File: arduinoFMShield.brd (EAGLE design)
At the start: 29.7 x 58.4 mm, 32 parts, among them IC1 ATMEGA168-MU, IC2 FT232RQ, X1 MINI-USB-32005-301, X2 R141426

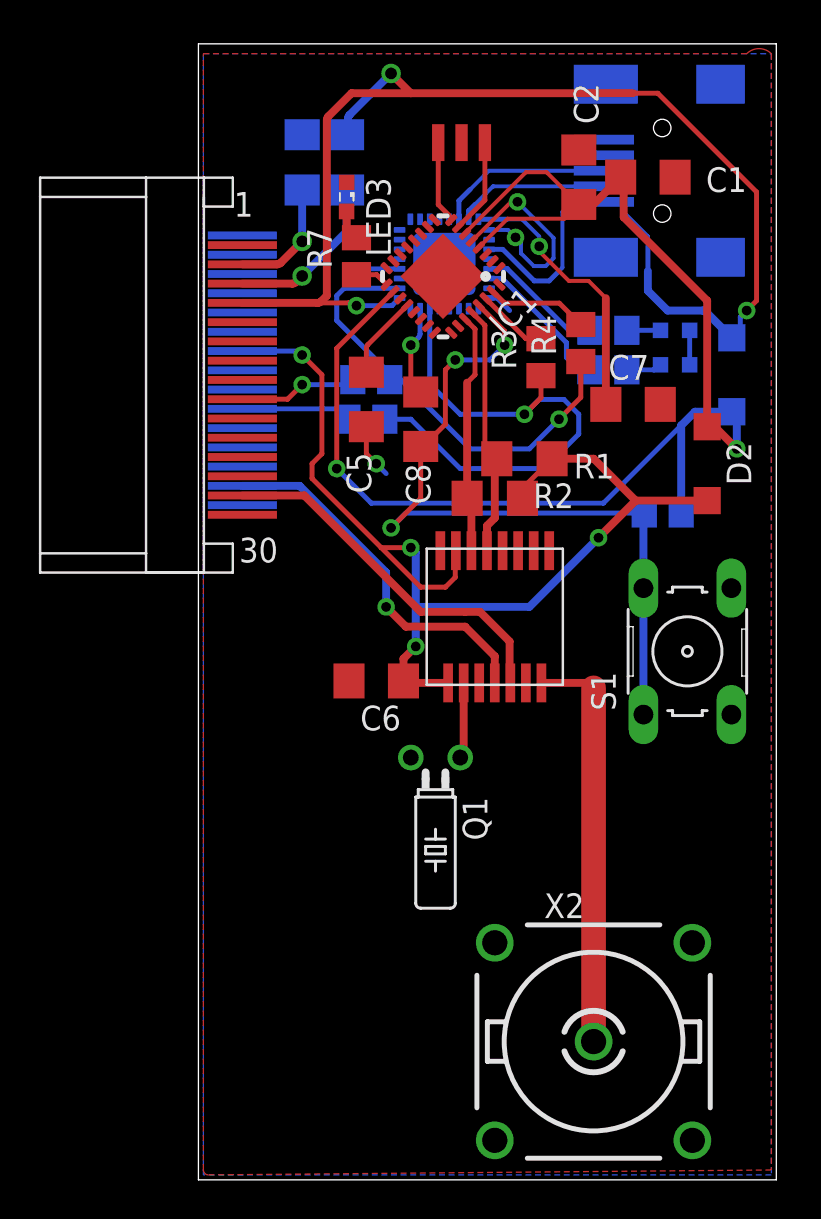
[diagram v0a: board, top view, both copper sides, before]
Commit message: 8/31/2013 Changed FTDI chip and atmega to bigger package for easier soldering. Add murata resonator
Signed-off-by: goose1987 <phamh1987@gmail.com>
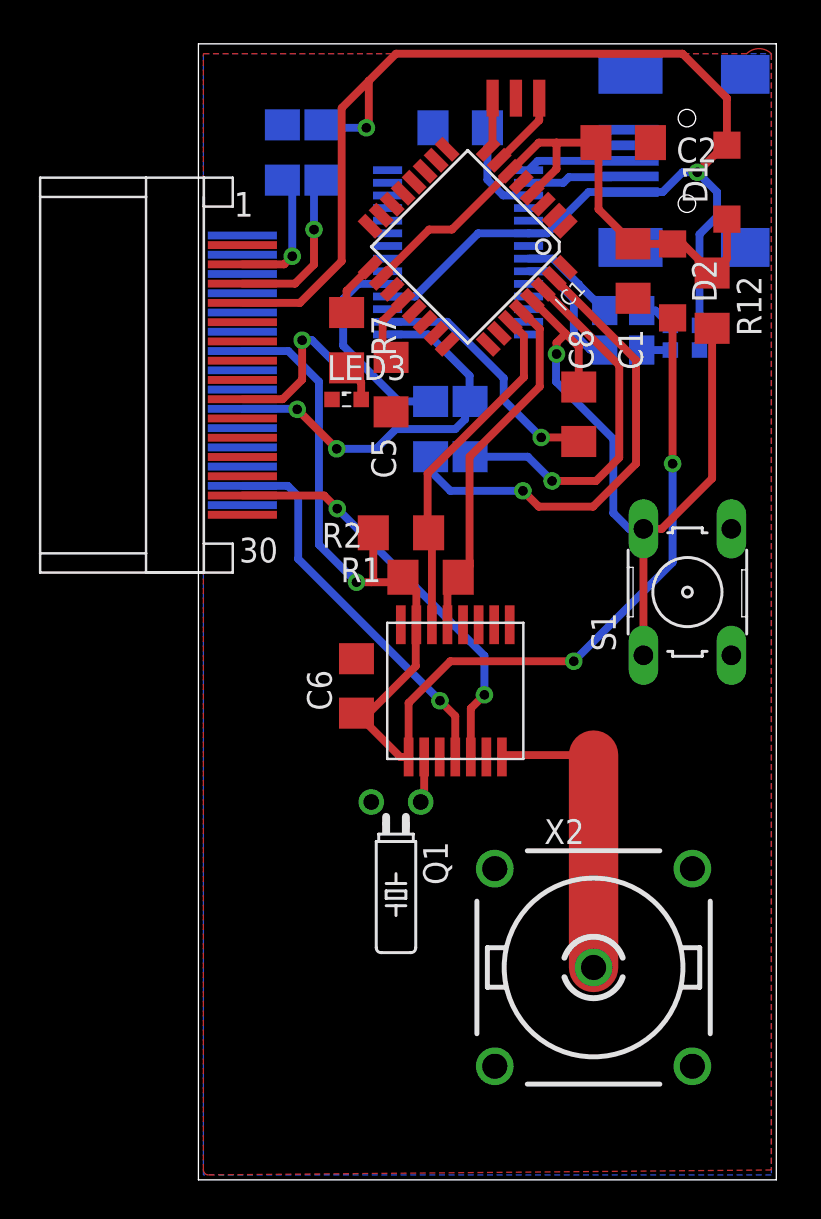
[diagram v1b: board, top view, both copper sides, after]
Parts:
- removed R10, R11: 1k, rcl:R0805
- IC1: value ATMEGA168-MU -> ATMEGA168-AU; device Arduino-AVR:MLF32 -> Arduino-AVR:TQFP32-08
- IC2: value FT232RQ -> FT232RL; device ftdichip:QFN32 -> ftdichip:SSOP28
- R12, R3, R4, R7: device rcl:R0805 -> rcl:R1206
- moved C7 16.8 mm to (11.7, 54.1), flipped to the bottom
- moved R12 11.2 mm to (24.6, 45.2), flipped to the top, turned to 270 degrees
- moved LED3 10.4 mm to (5.84, 40.1), turned to 0 degrees
- moved D1 9.91 mm to (25.4, 51.3), flipped to the top
- moved D2 9.56 mm to (22.6, 46.2)
- moved R4 8.90 mm to (10.2, 38.6), flipped to the bottom, turned to 270 degrees
- moved C8 8.13 mm to (17.8, 39.4), turned to 270 degrees
- moved R1 7.78 mm to (10.2, 31.0), turned to 180 degrees
- moved R3 5.19 mm to (12.2, 38.6), flipped to the bottom, turned to 270 degrees
- moved R2 5.14 mm to (8.64, 33.3), turned to 180 degrees
- moved C1 4.89 mm to (20.6, 46.7), turned to 90 degrees
- moved R7 4.35 mm to (5.84, 43.2), turned to 270 degrees
- moved U$1 4.32 mm to (11.4, 25.1)
- moved X2 3.81 mm to (18.5, 10.9)
- moved U$3 3.61 mm to (15.7, 55.6)
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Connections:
- removed net +5V: LED1.A, LED2.A
- removed net N$10: R11.1, U$2.18)
- removed net N$9: R10.1, U$2.19)
- net GND: now also IC2.18, IC2.21, IC2.25, IC2.7; no longer IC2.17, IC2.20, IC2.24, IC2.4
- net N$11: now also IC2.17; no longer IC2.16
- net N$16: now also IC2.2; no longer IC2.31
- net N$2: now also IC2.15; no longer IC2.14
- net N$3: now also IC2.16; no longer IC2.15
- net N$4: now also IC2.23; no longer IC2.22
- net N$5: now also IC2.22; no longer IC2.21
- net RX: now also IC2.1, U$2.19); no longer IC2.30, R10.2
- net TX: now also IC2.5, U$2.18); no longer IC2.2, R11.2
- net VUSB: now also IC2.20, IC2.4, LED1.A, LED2.A; no longer IC2.1, IC2.19
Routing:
- net VCC: track 73.1 -> 30.9 mm, vias 2 -> 0
- net N$13: track 5.24 -> 24.3 mm, vias 0 -> 1
- net GND: track 18.2 -> 0.00 mm, vias 3 -> 0
- net N$12: track 3.70 -> 19.0 mm, vias 0 -> 1
- net N$11: track 14.1 -> 5.12 mm, vias 1 -> 0
- net N$16: track 4.68 -> 13.0 mm
- net +3V3: track 57.6 -> 65.2 mm, vias 4 -> 3
- net RX: track 27.9 -> 20.4 mm, vias 1 -> 2
- net N$10: track 6.09 -> 0.00 mm, vias 1 -> 0
- net N$9: track 5.65 -> 0.00 mm
- net SDA: track 12.4 -> 18.0 mm
- net SCL: track 13.0 -> 18.5 mm
- net N$1: track 21.0 -> 15.7 mm
- net TX: track 23.6 -> 19.7 mm
- net N$2: track 9.04 -> 5.34 mm
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
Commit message: 8/31/2013 Fixed board dimension Moved silkscreen designator around for better visibility
Signed-off-by: goose1987 <phamh1987@gmail.com>
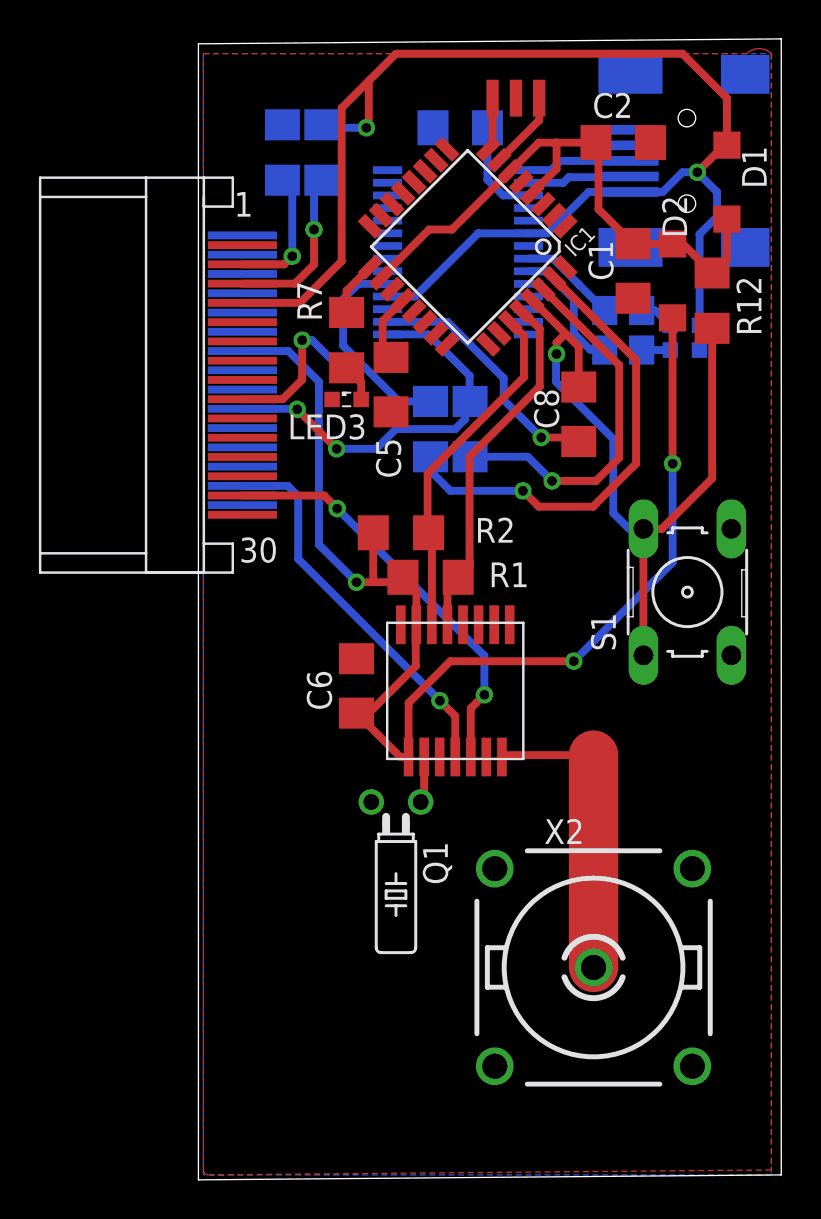
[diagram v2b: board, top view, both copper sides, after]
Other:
- board size 29.7 x 58.4 mm -> 30 x 58.7 mm
